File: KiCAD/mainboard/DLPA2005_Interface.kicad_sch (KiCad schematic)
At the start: 37 parts, among them IC2 DLPA2005ERSLT, P1P8V? TestPoint

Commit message: no more question marks!
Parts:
- removed L?: L, symbol Device:L
- removed R?: R_US, symbol Device:R_US
- removed TP?: TestPoint, symbol Connector:TestPoint
- added L2: L, symbol Device:L
- added R4: R_US, symbol Device:R_US
- added TP2: TestPoint, symbol Connector:TestPoint
- gave numbers to parts that had none: 32
- renumbered C22 to C169, IC2 to IC?
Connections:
- net GND: now also R4.1
- net at D18.1 (K), IC?.11 (SWN): now also L2.2
- net at IC?.13 (SWP): now also L2.1
- net at C200.1, IC?.21 (LS_OUT): now also TP2.1
- net at IC?.31 (LED_SEL0): now also R4.2
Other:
- moved on the sheet: C168, C169, C196, C197, C198, C199, C20, C200, C201, C21, C211, C212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

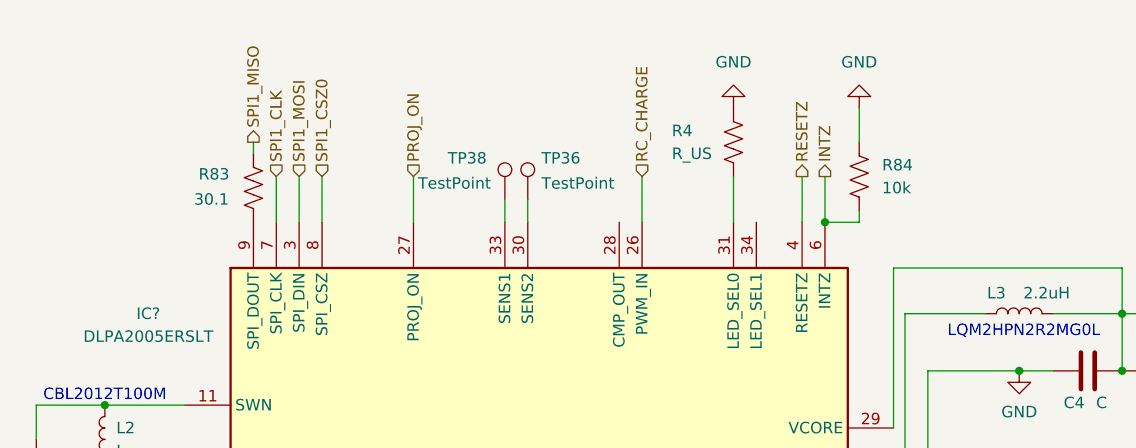
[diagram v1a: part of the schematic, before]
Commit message: replaced with 0805 all passives in DLPC
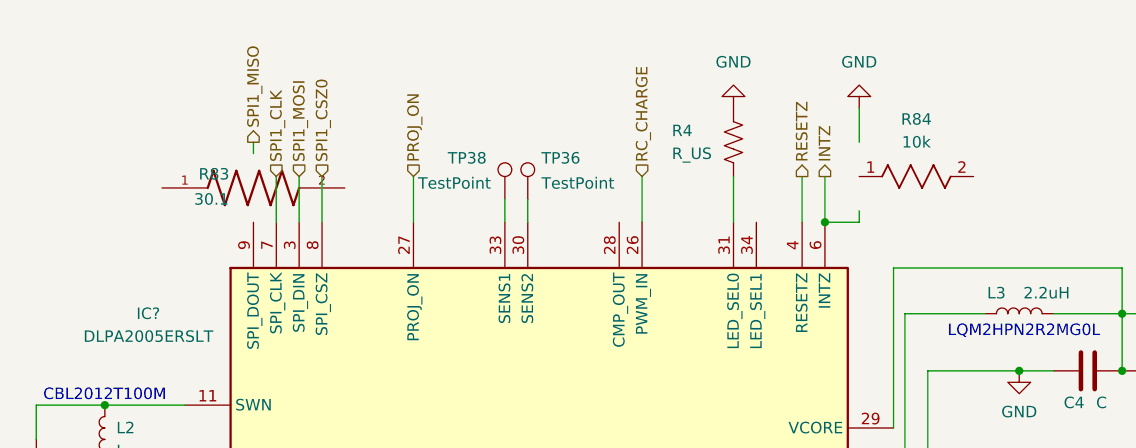
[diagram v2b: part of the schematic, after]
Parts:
- R83: footprint (none) -> RC0805FR-0730R1L:RESC2012X60N; symbol Device:R_US -> RC0805FR-0730R1L:RC0805FR-0730R1L; Check_prices (none) -> https://www.snapeda.com/parts/RC0805FR-0730R1L/Yageo/view-p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; Description_1 (none) -> 30.1 Ohms ±1% 0.125W, 1/8W Chip Resistor 0805 (2012 Metric)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; DigiKey_Part_Number (none) -> 311-30.1CRCT-ND; MF (none) -> Yageo; MP (none) -> RC0805FR-0730R1L; Manufacturer_Part_Number (none) -> RC0805FR-0730R1L; Package (none) -> 2012 Yageo; SnapEDA_Link (none) -> https://www.snapeda.com/parts/RC0805FR-0730R1L/Yageo/view-p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
- R84: footprint (none) -> STA_RMCF0805_STP; symbol Device:R_US -> RMCF0805FT10K0:RMCF0805FT10K0; Manufacturer_Part_Number (none) -> RMCF0805FT10K0
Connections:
- net GND: no longer R84.1
- net INTZ: no longer R84.2
- net SPI1_MISO: no longer R83.1
- net at IC?.9 (SPI_DOUT): no longer R83.2
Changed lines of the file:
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@@
 	)
 	(symbol
-		(lib_id "Device:R_US")
+		(lib_id "RC0805FR-0730R1L:RC0805FR-0730R1L")
 		(at 95.25 29.21 0)
 		(unit 1)
@@
 			)
 		)
-		(property "Footprint" ""
-			(at 96.266 29.464 90)
-			(effects
-				(font
-					(size 1.27 1.27)
-				)
+		(property "Footprint" "RC0805FR-0730R1L:RESC2012X60N"
+			(at 95.25 29.21 0)
+			(effects
+				(font
+					(size 1.27 1.27)
+				)
+				(justify bottom)
 				(hide yes)
 			)
@@
 					(size 1.27 1.27)
 				)
+				(hide yes)
+			)
+		)
+		(property "Manufacturer_Part_Number" "RC0805FR-0730R1L "
+			(at 95.25 29.21 0)
+			(effects
+				(font
+					(size 1.27 1.27)
+				)
+				(hide yes)
+			)
+		)
+		(property "DigiKey_Part_Number" "311-30.1CRCT-ND"
+			(at 95.25 29.21 0)
+			(effects
+				(font
+					(size 1.27 1.27)
+				)
+				(justify bottom)
+				(hide yes)
+			)
+		)
+		(property "SnapEDA_Link" "https://www.snapeda.com/parts/RC0805FR-0730R1L/Yageo/view-part/?ref=snap"
+			(at 95.25 29.21 0)
+			(effects
+				(font
+					(size 1.27 1.27)
+				)
+				(justify bottom)
+				(hide yes)
+			)
+		)
+		(property "Description_1" "30.1 Ohms ±1% 0.125W, 1/8W Chip Resistor 0805 (2012 Metric) Moisture Resistant Thick Film"
+			(at 95.25 29.21 0)
+			(effects
+				(font
+					(size 1.27 1.27)
+				)
+				(justify bottom)
+				(hide yes)
+			)
+		)
+		(property "MF" "Yageo"
+			(at 95.25 29.21 0)
+			(effects
+				(font
+					(size 1.27 1.27)
+				)
+				(justify bottom)
+				(hide yes)
+			)
+		)
+		(property "Package" "2012 Yageo"
+			(at 95.25 29.21 0)
+			(effects
+				(font
+					(size 1.27 1.27)
+				)
+				(justify bottom)
+				(hide yes)
+			)
+		)
+		(property "Check_prices" "https://www.snapeda.com/parts/RC0805FR-0730R1L/Yageo/view-part/?ref=eda"
+			(at 95.25 29.21 0)
+			(effects
+				(font
+					(size 1.27 1.27)
+				)
+				(justify bottom)
+				(hide yes)
+			)
+		)
+		(property "MP" "RC0805FR-0730R1L"
+			(at 95.25 29.21 0)
+			(effects
+				(font
+					(size 1.27 1.27)
+				)
+				(justify bottom)
 				(hide yes)
 			)
@@
 	)
 	(symbol
-		(lib_id "Device:R_US")
+		(lib_id "RMCF0805FT10K0:RMCF0805FT10K0")
 		(at 162.56 27.94 0)
 		(unit 1)
@@
 		(fields_autoplaced yes)
 		(property "Reference" "R84"
-			(at 165.1 26.6699 0)
-			(effects
-				(font
-					(size 1.27 1.27)
-				)
-				(justify left)
+			(at 168.91 21.59 0)
+			(effects
+				(font
+					(size 1.27 1.27)
+				)
 			)
 		)
 		(property "Value" "10k"
-			(at 165.1 29.2099 0)
-			(effects
-				(font
-					(size 1.27 1.27)
-				)
-				(justify left)
-			)
-		)
-		(property "Footprint" ""
-			(at 163.576 28.194 90)
-			(effects
-				(font
-					(size 1.27 1.27)
-				)
-				(hide yes)
-			)
-		)
-		(property "Datasheet" "~"
+			(at 168.91 24.13 0)
+			(effects
+				(font
+					(size 1.27 1.27)
+				)
+			)
+		)
+		(property "Footprint" "STA_RMCF0805_STP"
 			(at 162.56 27.94 0)
 			(effects
 				(font
 					(size 1.27 1.27)
+					(italic yes)
+				)
+				(hide yes)
+			)
+		)
+		(property "Datasheet" "RMCF0805FT10K0"
+			(at 162.56 27.94 0)
+			(effects
+				(font
+					(size 1.27 1.27)
+					(italic yes)
 				)
 				(hide yes)
@@
 			(at 162.56 27.94 0)
 			(effects
+				(font
+					(size 1.27 1.27)
+				)
+				(hide yes)
+			)
+		)
+		(property "Manufacturer_Part_Number" "RMCF0805FT10K0 "
+			(at 162.56 27.94 0)
+			(effects

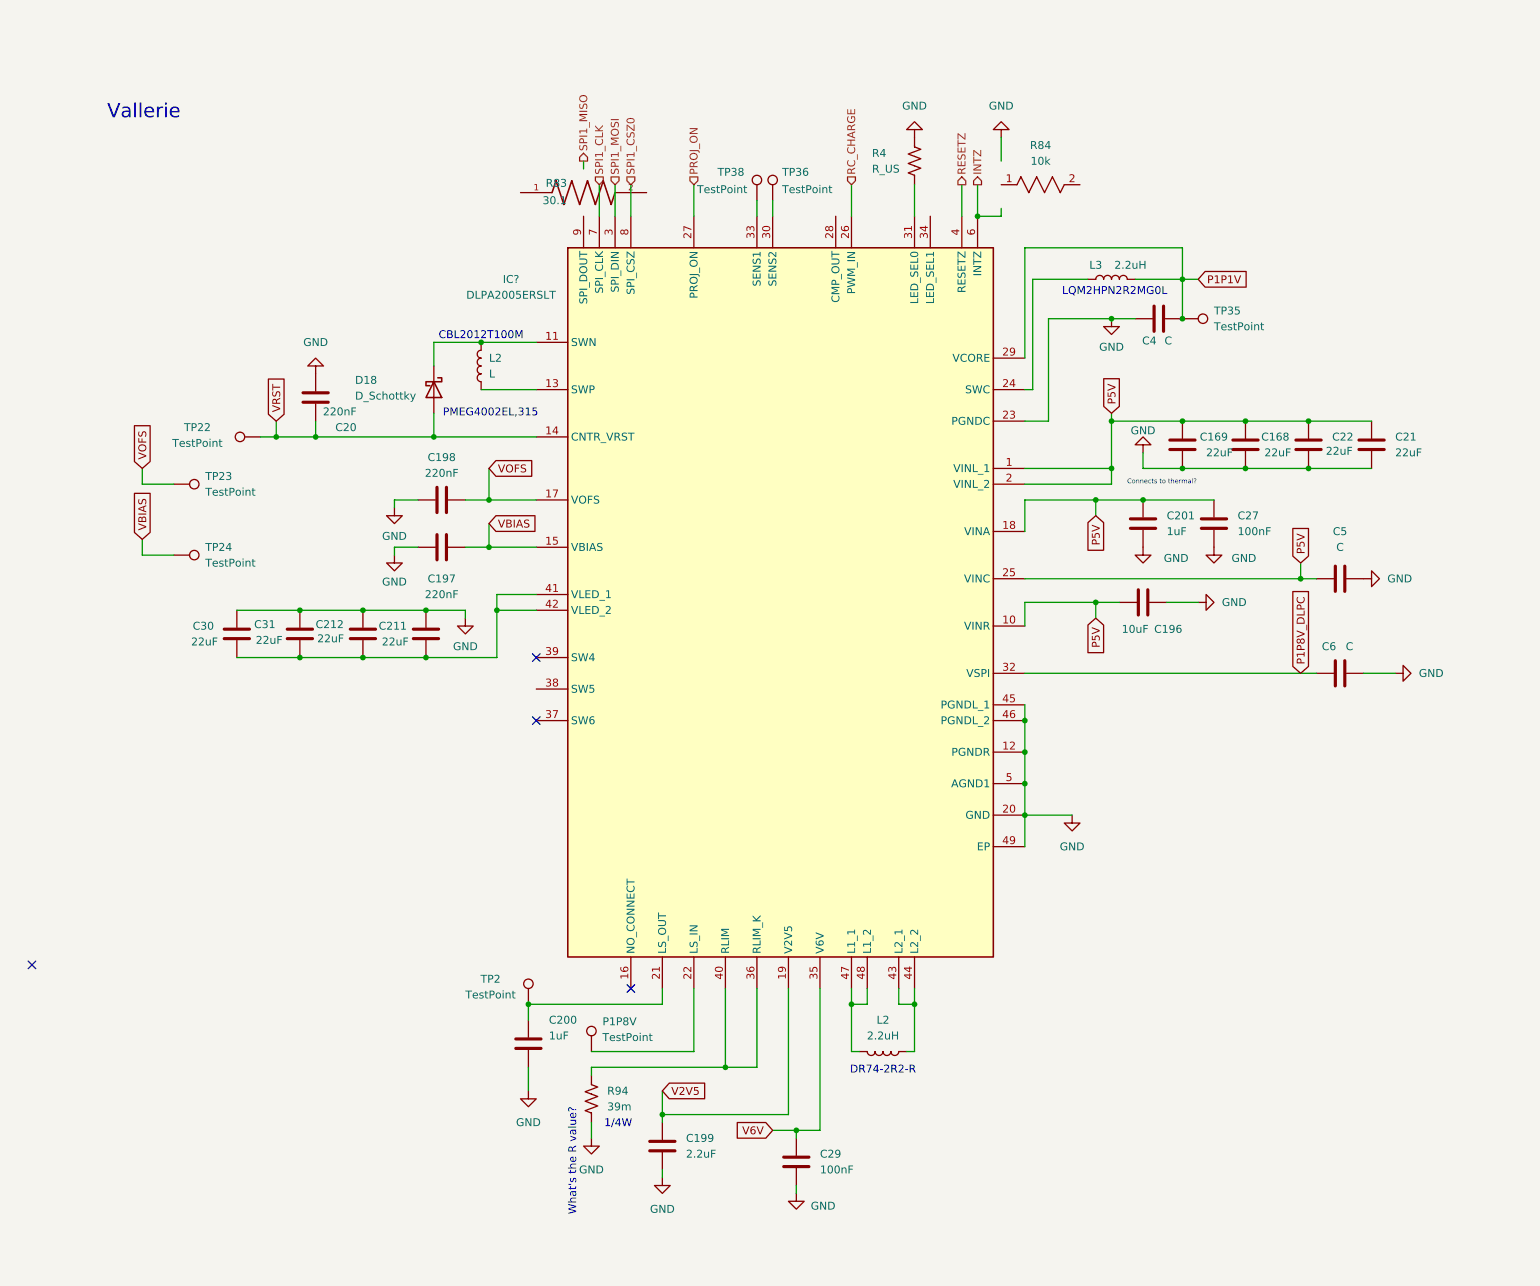
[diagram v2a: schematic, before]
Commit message: changes to all schematic files fixing ERC errors
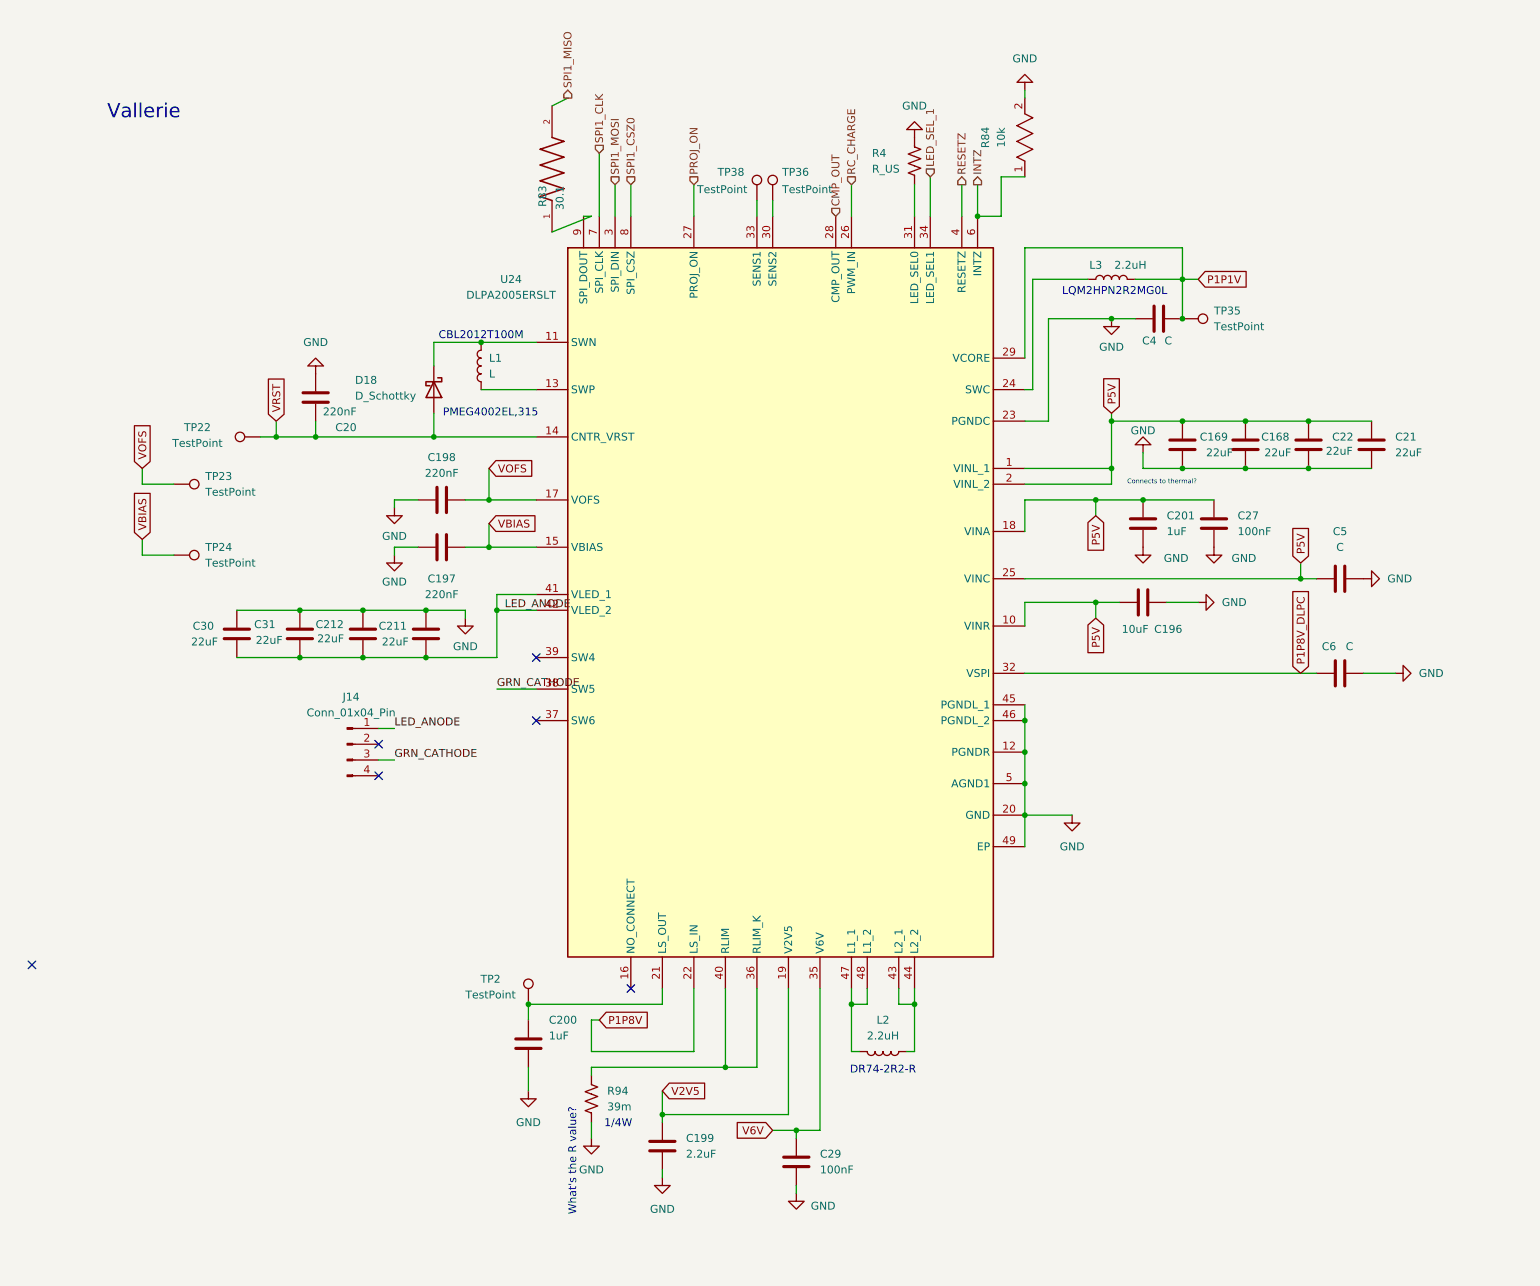
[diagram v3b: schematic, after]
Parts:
- removed P1P8V: TestPoint, symbol Connector:TestPoint
- added J14: Conn_01x04_Pin, Connector_PinHeader_2.54mm:PinHeader_1x04_P2.54mm_Vertical, symbol Connector:Conn_01x04_Pin
- gave numbers to parts that had none: 1
- renumbered L2 to L1
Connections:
- net GND: now also R84.2
- net INTZ: now also R84.1
- net SPI1_MISO: now also R83.2
- net P1P8V: now reaches U24.22 (LS_IN)
- net CMP_OUT: now reaches U24.28 (CMP_OUT)
- net LED_SEL_1: now reaches U24.34 (LED_SEL1)
- net GRN_CATHODE: now reaches U24.38 (SW5)
- net GRN_CATHODE: now also J14.3 (Pin_3)
- net LED_ANODE: now reaches C211.1, C212.1, C30.1, C31.1, U24.41 (VLED_1), U24.42 (VLED_2)
- net LED_ANODE: now also J14.1 (Pin_1)
- net at U24.9 (SPI_DOUT): now also R83.1
- no-connect marks 4 -> 6
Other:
- moved on the sheet: R83, R84

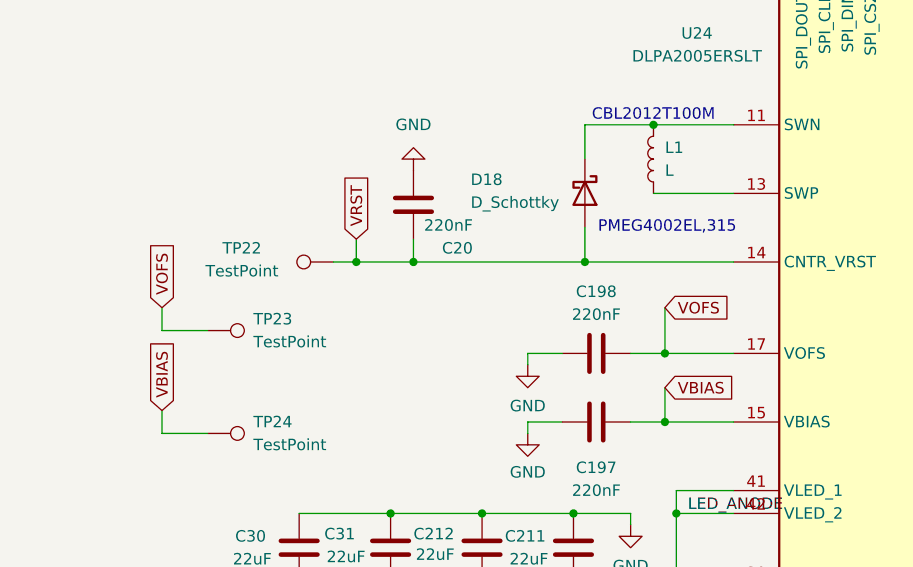
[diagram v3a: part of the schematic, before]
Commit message: meeting edits to DLPA and DLPC
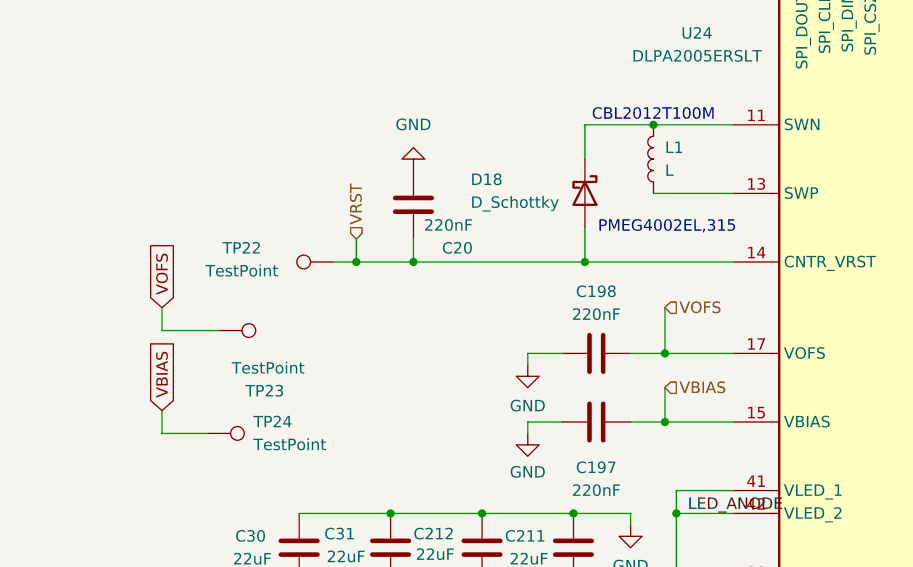
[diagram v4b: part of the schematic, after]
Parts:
- TP23, TP24: footprint (none) -> TestPoint:TestPoint_Pad_D1.5mm
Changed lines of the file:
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@@
 	(wire
 		(pts
-			(xy 29.21 76.2) (xy 24.13 76.2)
+			(xy 30.48 76.2) (xy 24.13 76.2)
 		)
 		(stroke
@@
 			)
 			(justify left bottom)
-		)
-	)
-	(global_label "VBIAS"
-		(shape input)
-		(at 80.01 82.55 0)
-		(fields_autoplaced yes)
-		(effects
-			(font
-				(size 1.27 1.27)
-			)
-			(justify left)
-		)
-		(property "Intersheetrefs" "${INTERSHEET_REFS}"
-			(at 88.2567 82.55 0)
-			(effects
-				(font
-					(size 1.27 1.27)
-				)
-				(justify left)
-				(hide yes)
-			)
 		)
 	)
@@
 	(global_label "VOFS"
 		(shape input)
-		(at 80.01 73.66 0)
-		(fields_autoplaced yes)
-		(effects
-			(font
-				(size 1.27 1.27)
-			)
-			(justify left)
-		)
-		(property "Intersheetrefs" "${INTERSHEET_REFS}"
-			(at 87.7124 73.66 0)
-			(effects
-				(font
-					(size 1.27 1.27)
-				)
-				(justify left)
-				(hide yes)
-			)
-		)
-	)
-	(global_label "VOFS"
-		(shape input)
 		(at 24.13 73.66 90)
 		(fields_autoplaced yes)
@@
 		)
 	)
-	(global_label "VRST"
-		(shape input)
-		(at 45.72 66.04 90)
-		(fields_autoplaced yes)
-		(effects
-			(font
-				(size 1.27 1.27)
-			)
-			(justify left)
-		)
-		(property "Intersheetrefs" "${INTERSHEET_REFS}"
-			(at 45.72 58.5191 90)
-			(effects
-				(font
-					(size 1.27 1.27)
-				)
-				(justify left)
-				(hide yes)
-			)
-		)
-	)
 	(global_label "P1P8V"
 		(shape input)
@@
 		)
 	)
+	(hierarchical_label "VRST"
+		(shape input)
+		(at 45.72 66.04 90)
+		(effects
+			(font
+				(size 1.27 1.27)
+			)
+			(justify left)
+		)
+	)
+	(hierarchical_label "VBIAS"
+		(shape input)
+		(at 80.01 82.55 0)
+		(effects
+			(font
+				(size 1.27 1.27)
+			)
+			(justify left)
+		)
+	)
+	(hierarchical_label "VOFS"
+		(shape input)
+		(at 80.01 73.66 0)
+		(effects
+			(font
+				(size 1.27 1.27)
+			)
+			(justify left)
+		)
+	)
 	(hierarchical_label "SPI1_CSZ0"
 		(shape input)
@@
 	)
 	(symbol
+		(lib_id "Connector:TestPoint")
+		(at 30.48 76.2 270)
+		(unit 1)
+		(exclude_from_sim no)
+		(in_bom yes)
+		(on_board yes)
+		(dnp no)
+		(property "Reference" "TP23"
+			(at 33.401 82.9309 90)
+			(effects
+				(font
+					(size 1.27 1.27)
+				)
+				(justify left)
+			)
+		)
+		(property "Value" "TestPoint"
+			(at 31.877 80.391 90)
+			(effects
+				(font
+					(size 1.27 1.27)
+				)
+				(justify left)
+			)
+		)
+		(property "Footprint" "TestPoint:TestPoint_Pad_D1.5mm"
+			(at 30.48 81.28 0)
+			(effects
+				(font
+					(size 1.27 1.27)
+				)
+				(hide yes)
+			)
+		)
+		(property "Datasheet" "~"
+			(at 30.48 81.28 0)
+			(effects
+				(font
+					(size 1.27 1.27)
+				)
+				(hide yes)
+			)
+		)
+		(property "Description" "test point"
+			(at 30.48 76.2 0)
+			(effects
+				(font
+					(size 1.27 1.27)
+				)
+				(hide yes)
+			)
+		)
+		(pin "1"
+		)
+		(instances
+			(project "mainboard"
+				(path "/38e83f42-2cf9-4799-a46f-ca415d95b90a/9cd29d54-68c1-4b23-aec1-57d737e6ea74"
+					(reference "TP23")
+					(unit 1)
+				)
+			)
+		)
+	)
+	(symbol
 		(lib_id "Device:C")
 		(at 201.93 69.85 0)
@@
 			)
 		)
-		(property "Footprint" ""
+		(property "Footprint" "TestPoint:TestPoint_Pad_D1.5mm"
 			(at 29.21 92.71 0)
 			(effects
@@
 					(unit 1)
 				)
-			)
-		)
-	)
-	(symbol
-		(lib_id "Connector:TestPoint")
-		(at 29.21 76.2 270)
-		(unit 1)
-		(exclude_from_sim no)
-		(in_bom yes)
-		(on_board yes)
-		(dnp no)
-		(fields_autoplaced yes)
-		(property "Reference" "TP23"
-			(at 34.29 74.9299 90)
-			(effects
-				(font
-					(size 1.27 1.27)
-				)
-				(justify left)
-			)
-		)
-		(property "Value" "TestPoint"
-			(at 34.29 77.4699 90)
-			(effects
-				(font
-					(size 1.27 1.27)
-				)
-				(justify left)
-			)
-		)
-		(property "Footprint" ""
-			(at 29.21 81.28 0)
-			(effects
-				(font
-					(size 1.27 1.27)
-				)
-				(hide yes)
-			)
-		)
-		(property "Datasheet" "~"
-			(at 29.21 81.28 0)
-			(effects
-				(font
-					(size 1.27 1.27)
-				)
-				(hide yes)
-			)
-		)
-		(property "Description" "test point"
-			(at 29.21 76.2 0)
-			(effects
-				(font
-					(size 1.27 1.27)
-				)
-				(hide yes)
-			)
-		)
-		(pin "1"
-		)
-		(instances
-			(project "mainboard"
-				(path "/38e83f42-2cf9-4799-a46f-ca415d95b90a/9cd29d54-68c1-4b23-aec1-57d737e6ea74"
-					(reference "TP23")
-					(unit 1)
-				)
